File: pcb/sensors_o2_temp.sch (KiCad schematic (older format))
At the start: 0 parts

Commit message: Sensors, misc peripherals
Added pressure sensor connections
Created project/schem for one of the pressure sensor daughterboard varieties
Added temperature and oxygen sensor inputs
Added misc. sheet (RTC, EEPROM, I2C mux)
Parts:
- added C?: 100nF 100V X7R, RespiraWorks_Std:C_0603_1608Metric, symbol Device:C
- added C?: 1uF 10V X7R, RespiraWorks_Std:C_0603_1608Metric, symbol Device:C
- added J?: Molex Micro-Fit, RespiraWorks_Std:Molex_Micro-Fit_3.0_43650-0315_1x03_P3.00mm_Vertical, symbol Connector_Generic:Conn_01x03
- added R?: 2.05K 1%, RespiraWorks_Std:R_0603_1608Metric, symbol Device:R
- added R? (x7): 10K 1%, RespiraWorks_Std:R_0603_1608Metric, symbol Device:R
- added R?: 1.5K 1%, RespiraWorks_Std:R_0603_1608Metric, symbol Device:R
- added R?: DNP, RespiraWorks_Std:R_0603_1608Metric, symbol Device:R
- added TP?: Stepper1_Temp, RespiraWorks_Std:TestPoint_Pad_2.0x2.0mm, symbol Connector:TestPoint
- added TP?: Stepper2_Temp, RespiraWorks_Std:TestPoint_Pad_2.0x2.0mm, symbol Connector:TestPoint
- added TP?: Blower_Temp, RespiraWorks_Std:TestPoint_Pad_2.0x2.0mm, symbol Connector:TestPoint
- added TP?: Batt_Temp, RespiraWorks_Std:TestPoint_Pad_2.0x2.0mm, symbol Connector:TestPoint
- added TP?: Spare_Temp, RespiraWorks_Std:TestPoint_Pad_2.0x2.0mm, symbol Connector:TestPoint
- added U?: INA333AIDGKR, RespiraWorks_Std:VSSOP-8_3.0x3.0mm_P0.65mm, symbol RespiraWorks:INA333AIDGKR
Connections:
- new net: R?.2, U?.1 (R1)
- new net: R?.2, U?.2 (-)
- new net: R?.2, U?.3 (+)
- new net: R?.1, R?.1, U?.6
- new net: R?.1, U?.8 (R1)
- new net: J?.3 (Pin_3), R?.1, R?.1, R?.1, R?.2
- new net: J?.1 (Pin_1), R?.1, R?.1, R?.2, R?.2
- new net +3.3V_Sns: C?.2, R?.2, R?.2, U?.7 (V+)
- new net Batt_Temp: TP?.1
- new net Blower_Temp: TP?.1
- new net GND: C?.1, C?.1, R?.1, R?.1, R?.2, U?.4 (V-), U?.5 (REF)
- new net Oxy_Level: C?.2, R?.2
- new net Spare_Temp: TP?.1
- new net Stepper1_Temp: TP?.1
- new net Stepper2_Temp: TP?.1
- no-connect marks 0 -> 1
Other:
- note added: "0 to 3.3V output = ??? to ???"
- note added: "LPF fc = 106 Hz"
- note added: "Optionally holds output low (10K or so)\nin case INA333 fails or its supply voltage\ndisappears"
- note added: "Rg"
- note added: "Rg = 100K/(Gain - 1)"
- note added: "Series input protection:\n200 pA max. input bias for INA333\n= 2 µV max. offset << 25 µV of\nINA333's own input offset"
- note added: "Teledyne R-24\nor equivalent"

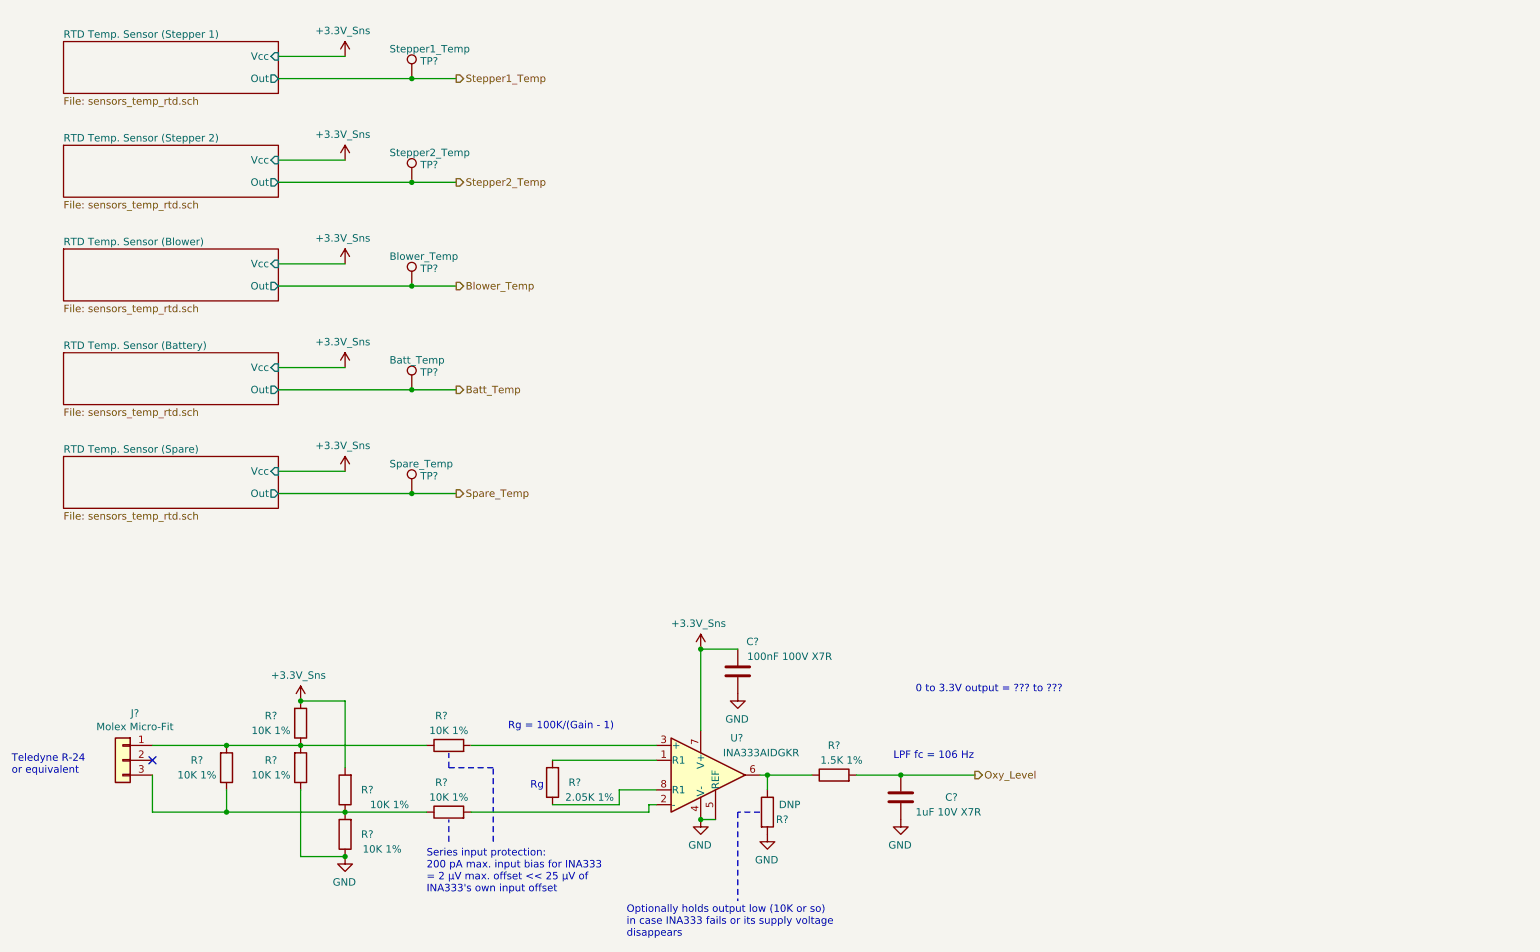
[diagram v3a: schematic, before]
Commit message: swapping RTD for NTC circuit.  Added gain clarifying notes on Oxygen sensor circuit.
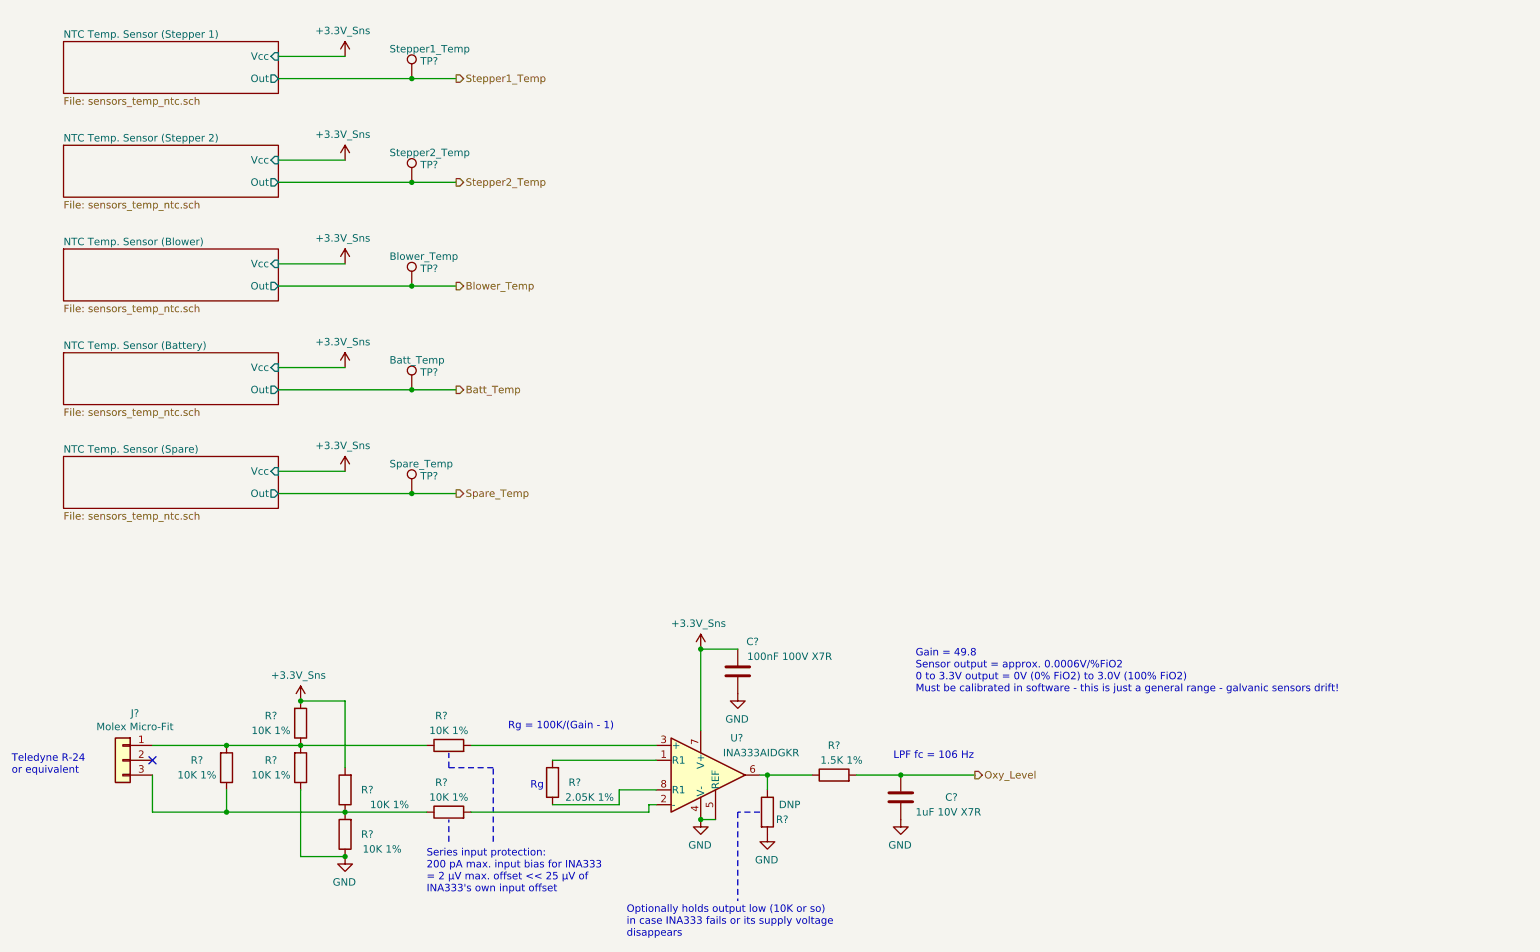
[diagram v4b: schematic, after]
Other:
- note added: "Gain = 49.8\nSensor output = approx. 0.0006V/%FiO2\n0 to 3.3V output = 0V (0% FiO2) to 3.0V (100% FiO2)\nMust be calibrated in software - this is just a general range - galvanic sensors drift!"
- note removed: "0 to 3.3V output = ??? to ???"
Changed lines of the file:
@@
 S 1100 1000 1450 350
 U 600F5EF3
-F0 "RTD Temp. Sensor (Stepper 1)" 50
-F1 "sensors_temp_rtd.sch" 50
+F0 "NTC Temp. Sensor (Stepper 1)" 50
+F1 "sensors_temp_ntc.sch" 50
 F2 "Out" O R 2550 1250 50
 F3 "Vcc" I R 2550 1100 50
@@
 S 1100 1700 1450 350
 U 600F7154
-F0 "RTD Temp. Sensor (Stepper 2)" 50
-F1 "sensors_temp_rtd.sch" 50
+F0 "NTC Temp. Sensor (Stepper 2)" 50
+F1 "sensors_temp_ntc.sch" 50
 F2 "Out" O R 2550 1950 50
 F3 "Vcc" I R 2550 1800 50
@@
 S 1100 2400 1450 350
 U 600F719E
-F0 "RTD Temp. Sensor (Blower)" 50
-F1 "sensors_temp_rtd.sch" 50
+F0 "NTC Temp. Sensor (Blower)" 50
+F1 "sensors_temp_ntc.sch" 50
 F2 "Out" O R 2550 2650 50
 F3 "Vcc" I R 2550 2500 50
@@
 S 1100 3100 1450 350
 U 600F71F1
-F0 "RTD Temp. Sensor (Battery)" 50
-F1 "sensors_temp_rtd.sch" 50
+F0 "NTC Temp. Sensor (Battery)" 50
+F1 "sensors_temp_ntc.sch" 50
 F2 "Out" O R 2550 3350 50
 F3 "Vcc" I R 2550 3200 50
@@
 S 1100 3800 1450 350
 U 600F723B
-F0 "RTD Temp. Sensor (Spare)" 50
-F1 "sensors_temp_rtd.sch" 50
+F0 "NTC Temp. Sensor (Spare)" 50
+F1 "sensors_temp_ntc.sch" 50
 F2 "Out" O R 2550 4050 50
 F3 "Vcc" I R 2550 3900 50
@@
 	5100 5850 4400 5850
 Text Notes 6850 5400 0    50   ~ 0
-0 to 3.3V output = ??? to ???
+Gain = 49.8\nSensor output = approx. 0.0006V/%FiO2\n0 to 3.3V output = 0V (0% FiO2) to 3.0V (100% FiO2)\nMust be calibrated in software - this is just a general range - galvanic sensors drift!
 $Comp
 L Device:R R?

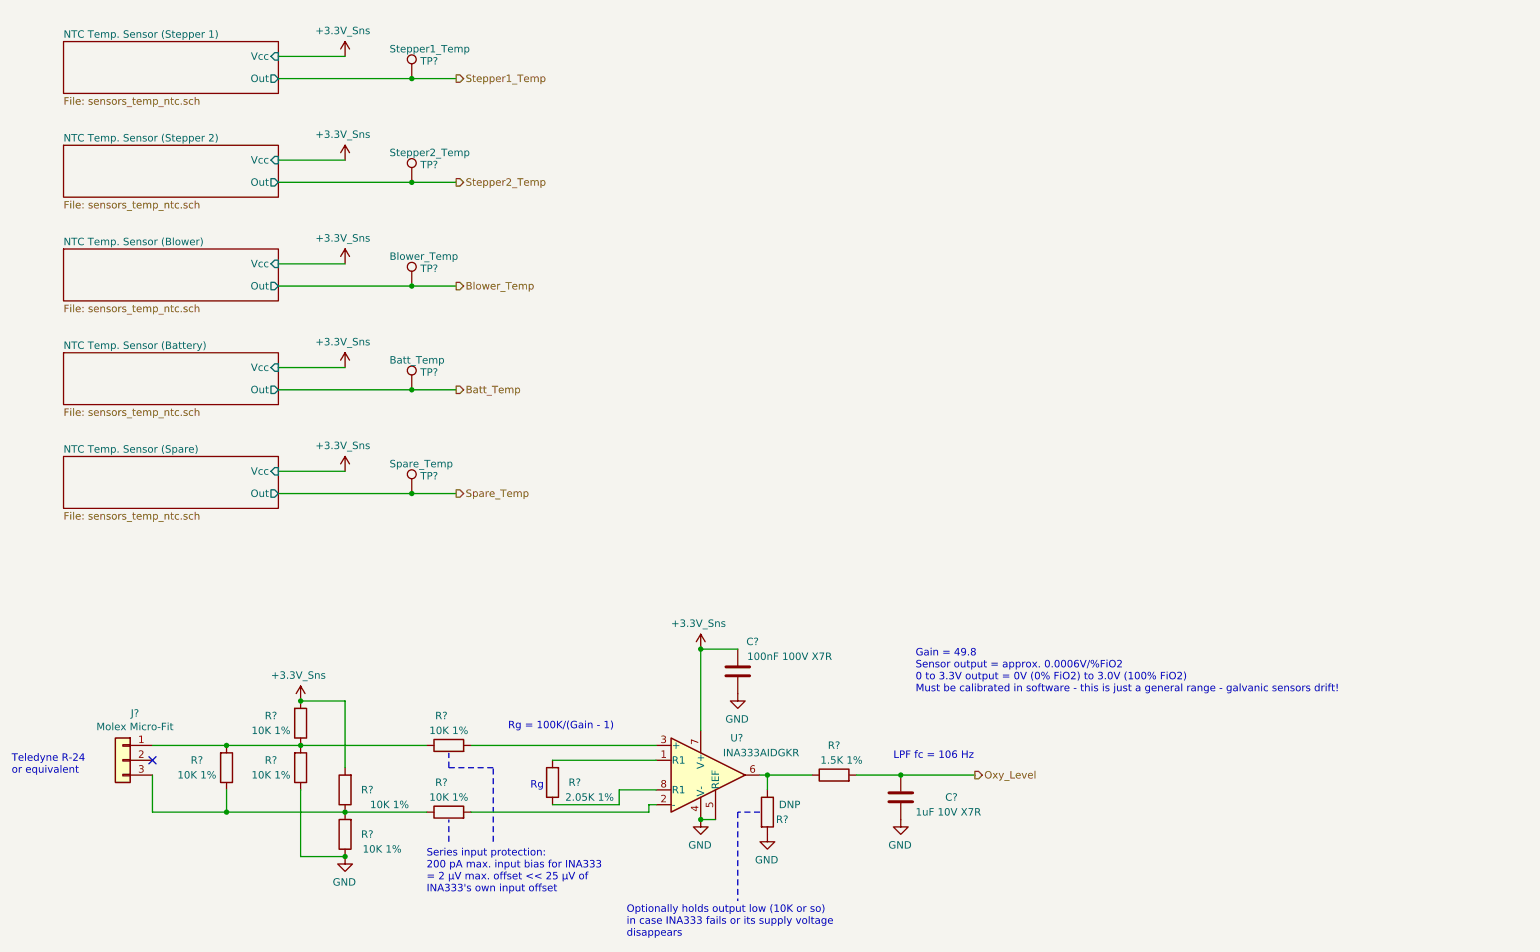
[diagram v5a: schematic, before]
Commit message: Monitoring
Finished top-level connections
Added separate SysMonADC for FPGA
Added voltage dividers for sensing input voltage levels
Broke out oxygen/temp sensor power to a hierarchical pin
Changed stepper STBY names to Reset to match ICD
Added OR'ed pull-downs to Stepper-nReset
Added FPGA alarm, external clamping for Low-Alarm-Bat signal
Added ability for FPGA to turn off 5V-UI
Changed CC's GND/GNDA connection from hardwired jumper to net tie
Added testpoints for probing
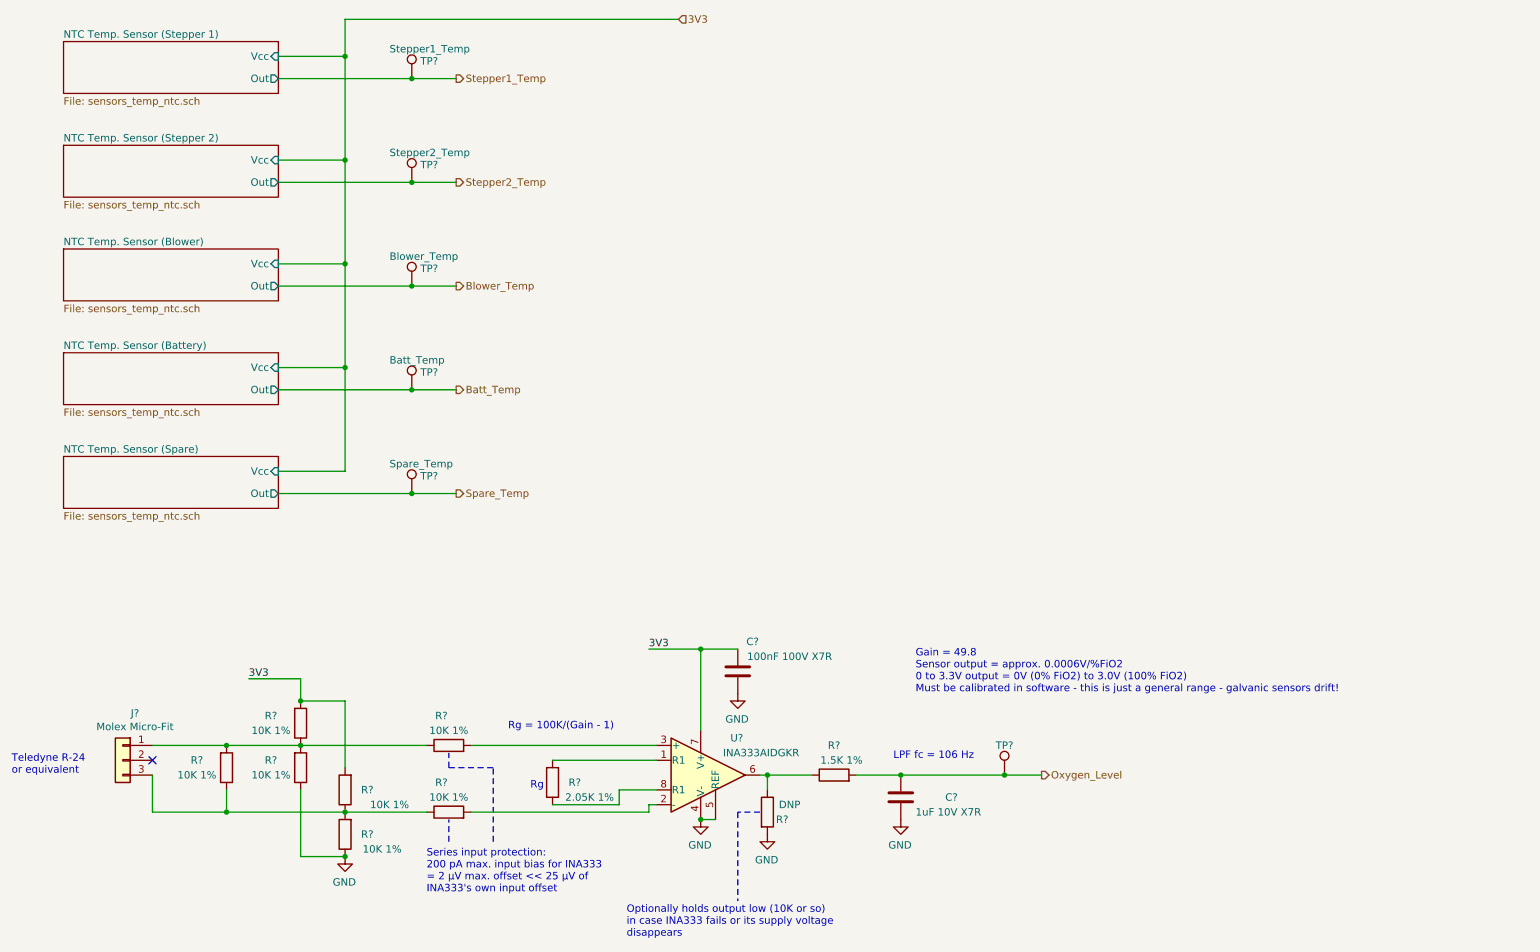
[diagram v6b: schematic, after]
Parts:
- added TP?: TP, symbol Connector:TestPoint
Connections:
- net +3.3V_Sns renamed 3V3
- net Oxy_Level renamed Oxygen_Level
- net Oxygen_Level: now also TP?.1
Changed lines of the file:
@@
 $Descr A4 11693 8268
 encoding utf-8
-Sheet 22 37
+Sheet 21 38
 Title "Oxygen and Temperature Sensors"
 Date ""
@@
 F3 "Vcc" I R 2550 3900 50
 $EndSheet
-$Comp
-L RespiraWorks:+3.3V_Sns #PWR?
-U 1 1 60107496
-P 3000 1100
-AR Path="/5FCD4EEA/600F5EF3/60107496" Ref="#PWR?"  Part="1"
-AR Path="/5FCD4EEA/60107496" Ref="#PWR?"  Part="1"
-F 0 "#PWR?" H 3000 1100 50  0001 C CNN
-F 1 "+3.3V_Sns" H 2985 1273 50  0000 C CNN
-F 2 "" H 3000 1100 50  0001 C CNN
-F 3 "" H 3000 1100 50  0001 C CNN
-	1    3000 1100
-	1    0    0    -1
-$EndComp
 Wire Wire Line
 	2550 1100 3000 1100
@@
 	3750 1250 3450 1250
 Connection ~ 3450 1250
-$Comp
-L RespiraWorks:+3.3V_Sns #PWR?
-U 1 1 6011C562
-P 3000 1800
-AR Path="/5FCD4EEA/600F5EF3/6011C562" Ref="#PWR?"  Part="1"
-AR Path="/5FCD4EEA/6011C562" Ref="#PWR?"  Part="1"
-F 0 "#PWR?" H 3000 1800 50  0001 C CNN
-F 1 "+3.3V_Sns" H 2985 1973 50  0000 C CNN
-F 2 "" H 3000 1800 50  0001 C CNN
-F 3 "" H 3000 1800 50  0001 C CNN
-	1    3000 1800
-	1    0    0    -1
-$EndComp
 Wire Wire Line
 	2550 1800 3000 1800
@@
 	3750 1950 3450 1950
 Connection ~ 3450 1950
-$Comp
-L RespiraWorks:+3.3V_Sns #PWR?
-U 1 1 6011C9C4
-P 3000 2500
-AR Path="/5FCD4EEA/600F5EF3/6011C9C4" Ref="#PWR?"  Part="1"
-AR Path="/5FCD4EEA/6011C9C4" Ref="#PWR?"  Part="1"
-F 0 "#PWR?" H 3000 2500 50  0001 C CNN
-F 1 "+3.3V_Sns" H 2985 2673 50  0000 C CNN
-F 2 "" H 3000 2500 50  0001 C CNN
-F 3 "" H 3000 2500 50  0001 C CNN
-	1    3000 2500
-	1    0    0    -1
-$EndComp
 Wire Wire Line
 	2550 2500 3000 2500
@@
 	3750 2650 3450 2650
 Connection ~ 3450 2650
-$Comp
-L RespiraWorks:+3.3V_Sns #PWR?
-U 1 1 6011CE53
-P 3000 3200
-AR Path="/5FCD4EEA/600F5EF3/6011CE53" Ref="#PWR?"  Part="1"
-AR Path="/5FCD4EEA/6011CE53" Ref="#PWR?"  Part="1"
-F 0 "#PWR?" H 3000 3200 50  0001 C CNN
-F 1 "+3.3V_Sns" H 2985 3373 50  0000 C CNN
-F 2 "" H 3000 3200 50  0001 C CNN
-F 3 "" H 3000 3200 50  0001 C CNN
-	1    3000 3200
-	1    0    0    -1
-$EndComp
 Wire Wire Line
 	2550 3200 3000 3200
@@
 	3750 3350 3450 3350
 Connection ~ 3450 3350
-$Comp
-L RespiraWorks:+3.3V_Sns #PWR?
-U 1 1 6011D298
-P 3000 3900
-AR Path="/5FCD4EEA/600F5EF3/6011D298" Ref="#PWR?"  Part="1"
-AR Path="/5FCD4EEA/6011D298" Ref="#PWR?"  Part="1"
-F 0 "#PWR?" H 3000 3900 50  0001 C CNN
-F 1 "+3.3V_Sns" H 2985 4073 50  0000 C CNN
-F 2 "" H 3000 3900 50  0001 C CNN
-F 3 "" H 3000 3900 50  0001 C CNN
-	1    3000 3900
-	1    0    0    -1
-$EndComp
 Wire Wire Line
 	2550 3900 3000 3900
@@
 	3750 4050 3450 4050
 Connection ~ 3450 4050
-Text HLabel 7250 5950 2    50   Output ~ 0
-Oxy_Level
+Text HLabel 7700 5950 2    50   Output ~ 0
+Oxygen_Level
 $Comp
 L RespiraWorks:INA333AIDGKR U?
@@
 Connection ~ 6750 5950
 Wire Wire Line
-	6750 5950 7250 5950
+	6750 5950 7450 5950
 Text Notes 6700 5850 0    50   ~ 0
 LPF fc = 106 Hz
@@
 NoConn ~ 1700 5850
 $Comp
-L RespiraWorks:+3.3V_Sns #PWR?
-U 1 1 60148A3F
-P 5400 5100
-AR Path="/5FCD4EEA/600F5EF3/60148A3F" Ref="#PWR?"  Part="1"
-AR Path="/5FCD4EEA/60148A3F" Ref="#PWR?"  Part="1"
-F 0 "#PWR?" H 5400 5100 50  0001 C CNN
-F 1 "+3.3V_Sns" H 5385 5273 50  0000 C CNN
-F 2 "" H 5400 5100 50  0001 C CNN
-F 3 "" H 5400 5100 50  0001 C CNN
-	1    5400 5100
-	1    0    0    -1
-$EndComp
-Connection ~ 5400 5100
-$Comp
-L RespiraWorks:+3.3V_Sns #PWR?
-U 1 1 60148D99
-P 2700 5450
-AR Path="/5FCD4EEA/600F5EF3/60148D99" Ref="#PWR?"  Part="1"
-AR Path="/5FCD4EEA/60148D99" Ref="#PWR?"  Part="1"
-F 0 "#PWR?" H 2700 5450 50  0001 C CNN
-F 1 "+3.3V_Sns" H 2685 5623 50  0000 C CNN
-F 2 "" H 2700 5450 50  0001 C CNN
-F 3 "" H 2700 5450 50  0001 C CNN
-	1    2700 5450
-	1    0    0    -1
-$EndComp
-$Comp
 L Device:R R?
 U 1 1 601505E1
@@
 Wire Wire Line
 	2700 5450 3000 5450
-Connection ~ 2700 5450
 $Comp
 L Device:R R?
@@
 Wire Wire Line
 	2200 6200 3000 6200
+Text HLabel 5250 850  2    50   Input ~ 0
+3V3
+Wire Wire Line
+	3000 1100 3000 850
+Wire Wire Line
+	3000 850  5250 850
+Wire Wire Line
+	2700 5450 2700 5300
+Wire Wire Line
+	2700 5300 2350 5300
+Connection ~ 2700 5450
+Text Label 2350 5300 0    50   ~ 0
+3V3
+Wire Wire Line
+	5400 5100 5050 5100
+Text Label 5050 5100 0    50   ~ 0
+3V3
+Connection ~ 5400 5100
+Wire Wire Line
+	3000 3900 3000 3200
+Connection ~ 3000 1100
+Connection ~ 3000 1800
+Wire Wire Line
+	3000 1800 3000 1100
+Connection ~ 3000 2500
+Wire Wire Line
+	3000 2500 3000 1800
+Connection ~ 3000 3200
+Wire Wire Line
+	3000 3200 3000 2500
+$Comp
+L Connector:TestPoint TP?
+U 1 1 60F7C3BE
+P 7450 5950
+AR Path="/5FCD50A5/60F7C3BE" Ref="TP?"  Part="1"
+AR Path="/6052CC9F/60F7C3BE" Ref="TP?"  Part="1"
+AR Path="/60F7C3BE" Ref="TP?"  Part="1"
+AR Path="/5FCD4D18/60F7C3BE" Ref="TP?"  Part="1"
+AR Path="/5FCD4B8E/60F7C3BE" Ref="TP?"  Part="1"
+F 0 "TP?" H 7450 6150 50  0000 C CNN
+F 1 "TP" V 7500 6000 50  0001 C CNN
+F 2 "" H 7650 5950 50  0001 C CNN
+F 3 "~" H 7650 5950 50  0001 C CNN
+	1    7450 5950
+	1    0    0    -1
+$EndComp
+Connection ~ 7450 5950
+Wire Wire Line
+	7450 5950 7700 5950
 $EndSCHEMATC
